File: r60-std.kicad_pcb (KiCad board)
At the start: 2 copper layers, 285.8 x 95.3 mm, 146 parts, among them K0 K_ESC, K0A1 K_0, K0B1 K_MIN, K0C1 K_EQL, K0D1 K_BS, K1 K_1, K10 K_TAB, K11 K_Q, K12 K_W, K13 K_E, K14 K_R, K15 K_T, K16 K_Y, K17 K_U, K18 K_I, K19 K_O, K1A1 K_P, K1B1 K_OBR, K1C1 K_CBR, K1D1 K_BSL, K2 K_2, K20 K_CAP, K21 K_A, K22 K_S, K23 K_D, K24 K_F, K25 K_G, K26 K_H, K27 K_J, K28 K_K, K29 K_L, K2A1 K_COL, K2B1 K_QOT, K2C1 K_ENT, K3 K_3, K30 K_LSH, K31 K_Z, K32 K_X, K33 K_C, K34 K_V, K35 K_B, K36 K_N, K37 K_M, K38 K_COM, K39 K_DOT, K3A1 K_QUE, K3B1 K_RSH, K4 K_4, K40 K_LCL, K41 K_LWN, K42 K_LAL, K45 K_SP, K48 K_RFN, K49 K_RALT, K4A1 K_RWIN, K4B1 K_RCTL, K5 K_5, K6 K_6, K7 K_7, K8 K_8, K9 K_9, P1 USB_B, P2 SPKR, SW1 SW_Push, U1 ATmega32U4-AU, Y1 16MHz

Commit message: Change cut edge holes to slot cuts
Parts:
- removed the REF** at (28.6, 100.0)
- removed the REF** at (314.3, 100.0)
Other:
- outline, holes or cut-outs redrawn
- board text added: "R60 Standard Board Rev 1.1"
- board text removed: "R60 Standard Board Rev A"
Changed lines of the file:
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@@
     (links 230)
     (no_connects 0)
-    (area 22.025 41.274999 320.875 138.420451)
+    (area 28.499999 42.787499 314.400001 138.187501)
     (thickness 1.6)
-    (drawings 11)
+    (drawings 19)
     (tracks 878)
     (zones 0)
-    (modules 146)
+    (modules 144)
     (nets 93)
   )
   (page USLegal)
+  (title_block
+    (title r60-std)
+    (date 2017-08-19)
+    (rev 1.1)
+  )
   (layers
     (0 F.Cu signal)
@@
     (visible_elements FFFFFF7F)
     (pcbplotparams
-      (layerselection 0x010f0_80000001)
+      (layerselection 0x010fc_80000001)
       (usegerberextensions true)
       (excludeedgelayer true)
@@
     (pad 4 thru_hole circle (at 0 0) (size 7 7) (drill oval 5.2 2.7) (layers *.Cu *.Mask))
   )
-  (module Mounting_Holes:MountingHole_2.7mm_M2.5 locked (layer F.Cu)
-    (at 28.575 100.0125)
-    (descr "Mounting Hole 2.7mm, no annular, M2.5")
-    (tags "mounting hole 2.7mm no annular m2.5")
-    (fp_text reference REF** (at 0 -3.7) (layer F.SilkS)
-      (effects (font (size 1 1) (thickness 0.15)))
-    )
-    (fp_text value "" (at 0 3.7) (layer F.Fab)
-      (effects (font (size 1 1) (thickness 0.15)))
-    )
-    (fp_circle (center 0 0) (end 2.7 0) (layer Cmts.User) (width 0.15))
-    (fp_circle (center 0 0) (end 2.95 0) (layer F.CrtYd) (width 0.05))
-    (pad 2 thru_hole oval (at 0 0) (size 12.7 5) (drill oval 10 2.7) (layers *.Cu *.Mask))
-  )
-  (module Mounting_Holes:MountingHole_2.7mm_M2.5 (layer F.Cu)
-    (at 314.325 100.0125)
-    (descr "Mounting Hole 2.7mm, no annular, M2.5")
-    (tags "mounting hole 2.7mm no annular m2.5")
-    (fp_text reference REF** (at 0 -3.7) (layer F.SilkS)
-      (effects (font (size 1 1) (thickness 0.15)))
-    )
-    (fp_text value "" (at 0 3.7) (layer F.Fab)
-      (effects (font (size 1 1) (thickness 0.15)))
-    )
-    (fp_circle (center 0 0) (end 2.7 0) (layer Cmts.User) (width 0.15))
-    (fp_circle (center 0 0) (end 2.95 0) (layer F.CrtYd) (width 0.05))
-    (pad 6 thru_hole oval (at 0 0) (size 12.7 5) (drill oval 10 2.7) (layers *.Cu *.Mask))
-  )
   (module Diodes_THT:D_A-405_P7.62mm_Horizontal (layer F.Cu)
     (at 42.148125 61.9125 180)
@@
       (xy -10.45728 7.127474) (xy -10.4013 7.132925) (xy -10.303849 7.132455)) (layer B.SilkS) (width 0.01))
   )
+  (gr_line (start 314.3238 45.24374) (end 314.3238 98.702578) (layer Edge.Cuts) (width 0.15))
+  (gr_line (start 314.3238 135.73086) (end 314.3238 101.321942) (layer Edge.Cuts) (width 0.15))
+  (gr_arc (start 310.632878 100.01226) (end 310.632878 101.321942) (angle 180) (layer Edge.Cuts) (width 0.15))
+  (gr_line (start 314.3238 101.321942) (end 310.632878 101.321942) (layer Edge.Cuts) (width 0.15))
+  (gr_line (start 314.3238 98.702578) (end 310.632878 98.702578) (layer Edge.Cuts) (width 0.15))
+  (gr_line (start 28.575 98.702578) (end 28.575 45.24374) (layer Edge.Cuts) (width 0.15))
+  (gr_line (start 28.575 135.73086) (end 28.575 101.321942) (layer Edge.Cuts) (width 0.15))
+  (gr_arc (start 32.14686 100.01226) (end 32.265922 98.702578) (angle 170.0419294) (layer Edge.Cuts) (width 0.15))
+  (gr_line (start 28.575 101.321942) (end 32.265922 101.321942) (layer Edge.Cuts) (width 0.15))
+  (gr_line (start 28.575 98.702578) (end 32.265922 98.702578) (layer Edge.Cuts) (width 0.15))
   (gr_text http://github.com/rpedde/r60-std (at 198.501 123.6345) (layer B.SilkS)
     (effects (font (size 1.5 1.5) (thickness 0.3)) (justify mirror))
   )
-  (gr_text "R60 Standard Board Rev A" (at 197.739 126.4285) (layer B.SilkS)
+  (gr_text "R60 Standard Board Rev 1.1" (at 197.739 126.4285) (layer B.SilkS)
     (effects (font (size 1.5 1.5) (thickness 0.3)) (justify mirror))
   )
@@
   )
   (gr_line (start 311.94375 138.1125) (end 30.95625 138.1125) (angle 90) (layer Edge.Cuts) (width 0.15))
-  (gr_line (start 314.325 45.24375) (end 314.325 135.73125) (angle 90) (layer Edge.Cuts) (width 0.15))
   (gr_line (start 30.95625 42.8625) (end 311.94375 42.8625) (angle 90) (layer Edge.Cuts) (width 0.15))
-  (gr_line (start 28.575 135.73125) (end 28.575 45.24375) (angle 90) (layer Edge.Cuts) (width 0.15))
   (gr_arc (start 30.95625 135.73125) (end 30.95625 138.1125) (angle 90) (layer Edge.Cuts) (width 0.15))
   (gr_arc (start 311.94375 135.73125) (end 314.325 135.73125) (angle 90) (layer Edge.Cuts) (width 0.15))

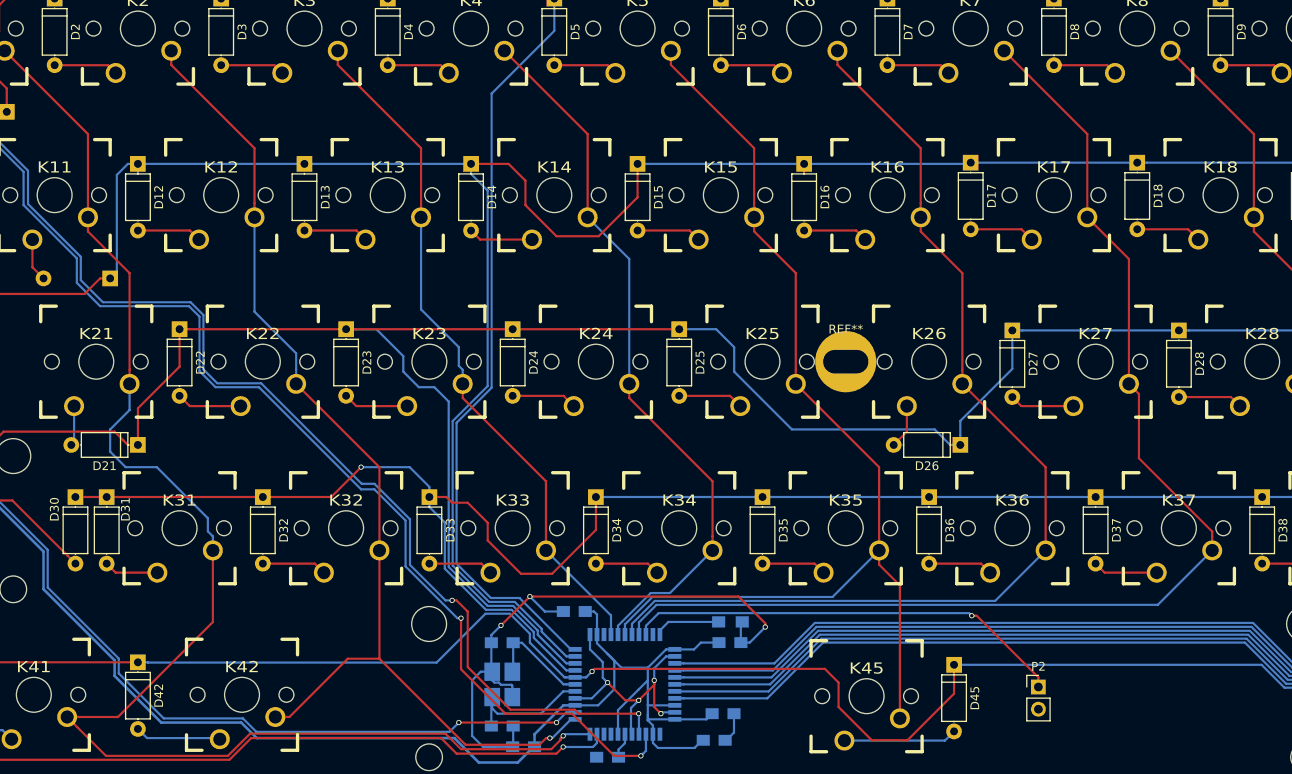
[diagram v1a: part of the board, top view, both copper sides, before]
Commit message: Fix silkscreen, move speaker connector, add speaker hardware
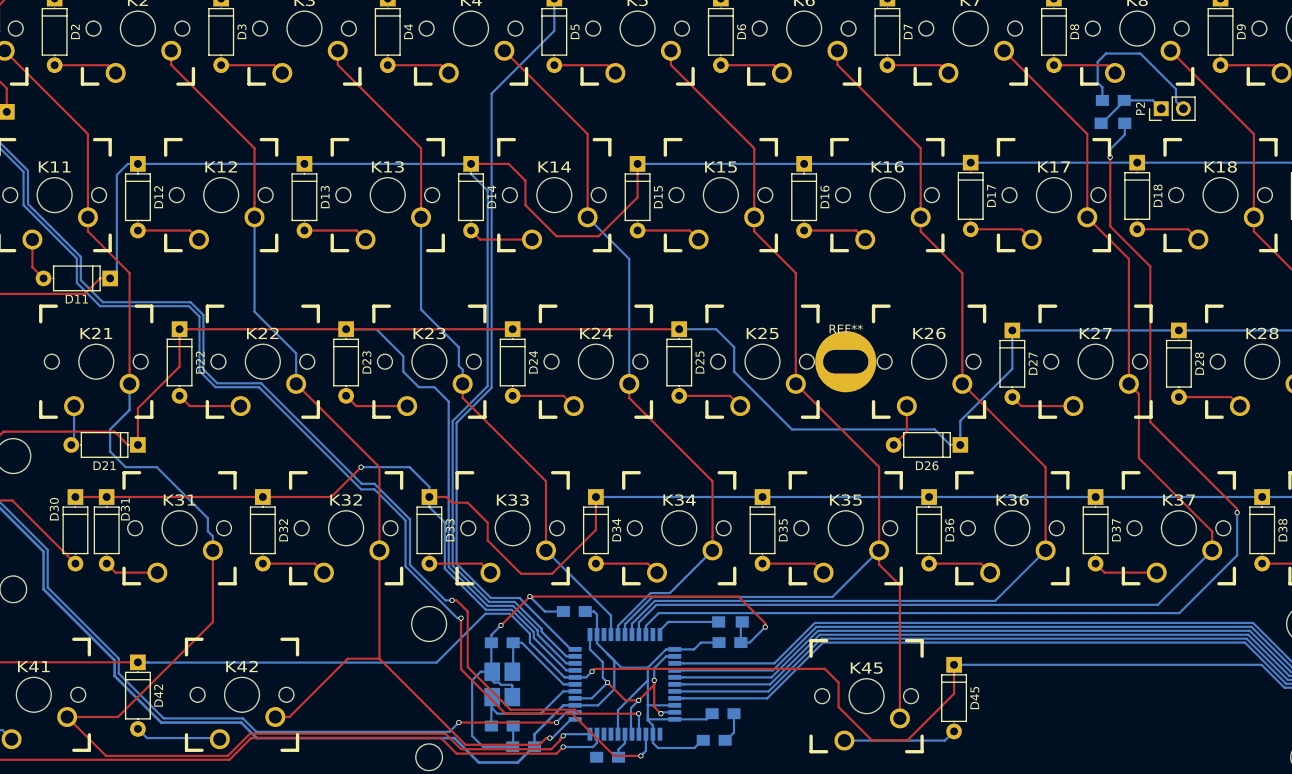
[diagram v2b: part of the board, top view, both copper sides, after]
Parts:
- added C9: .1uF, Capacitors_SMD:C_0805_HandSoldering, B.Cu at (187.8, 60.6)
- added R5: 22, Resistors_SMD:R_0805_HandSoldering, B.Cu at (187.7, 63.2)
- D11: moved to F.Cu
- moved P2 67.6 mm to (193.2, 61.6), turned to 90 degrees
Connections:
- P2 pad 1: Net-(P2-Pad1) -> Net-(C9-Pad1)
- U1 pad 31: Net-(P2-Pad1) -> Net-(R5-Pad1)
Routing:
- net Net-(R5-Pad1): track 0.00 -> 128.1 mm, vias 0 -> 2
- net Net-(P2-Pad1): track 50.6 -> 0.00 mm, vias 1 -> 0
- net GND: track 156.1 -> 174.4 mm
- net Net-(C9-Pad1): track 0.00 -> 8.39 mm
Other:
- board text added: "R60 Standard Board Rev 1.2"
- board text removed: "R60 Standard Board Rev 1.1"

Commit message: start on r2.0 board
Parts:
- C1, C2, C3, C4, C5, C6, C7, C8, C9: footprint Capacitors_SMD:C_0805_HandSoldering -> Capacitors_SMD:C_0805
- D0, D0A1, D0B1, D0C1, D0D1, D1, D10, D11, D12, D13, D14, D15, D16, D17, D18, D19, D1A1, D1B1, D1C1, D1D1, D2, D20, D21, D22, D23, D24, D25, D26, D27, D28, D29, D2A1, D2B1, D2C1, D3, D30, D31, D32, D33, D34, D35, D36, D37, D38, D39, D3A1, D3B1, D4, D40, D41, D42, D45, D48, D49, D4A1, D4B1, D5, D6, D7, D8, D9: footprint Diodes_THT:D_A-405_P7.62mm_Horizontal -> Diodes_SMD:D_SOD-323; moved to B.Cu
- R1, R2, R3, R4, R5: footprint Resistors_SMD:R_0805_HandSoldering -> Resistors_SMD:R_0805
- Y1: footprint Crystals:Crystal_SMD_3225-4pin_3.2x2.5mm_HandSoldering -> Crystals:Crystal_SMD_3225-4pin_3.2x2.5mm
- moved D2C1 23.5 mm to (294.1, 96.4), turned to 180 degrees
- moved D0D1 23.5 mm to (297.7, 58.3), turned to 180 degrees
- moved D3B1 23.5 mm to (289.3, 115.5), turned to 180 degrees
- moved D30 20.2 mm to (51.2, 115.5), turned to 180 degrees
- moved D20 19.4 mm to (46.4, 96.4), turned to 180 degrees
- moved D42 16.3 mm to (89.3, 134.5), turned to 180 degrees
- moved D4B1 16.2 mm to (303.6, 134.5), turned to 180 degrees
- moved D4A1 16.1 mm to (279.8, 134.5), turned to 180 degrees
- moved D17 14.4 mm to (182.2, 77.4), turned to 180 degrees
- moved D1A1 14.4 mm to (239.3, 77.4), turned to 180 degrees
- moved D1B1 14.4 mm to (258.4, 77.4), turned to 180 degrees
- moved D2B1 14.4 mm to (263.1, 96.4), turned to 180 degrees
- moved D18 14.4 mm to (201.2, 77.4), turned to 180 degrees
- moved D19 14.4 mm to (220.3, 77.4), turned to 180 degrees
- moved D1C1 14.4 mm to (277.4, 77.4), turned to 180 degrees
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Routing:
- net GND: track 174.4 -> 77.3 mm, vias 9 -> 7
- net /R4: track 261.4 -> 311.9 mm, vias 1 -> 2
- net Net-(R5-Pad1): track 128.1 -> 159.0 mm
- net Net-(D30-Pad2): track 32.4 -> 3.32 mm
- net /R2: track 330.3 -> 305.5 mm, vias 0 -> 4
- net /R1: track 350.3 -> 332.0 mm, vias 0 -> 4
- net /R0: track 336.4 -> 352.1 mm, vias 0 -> 4
- net Net-(R1-Pad2): track 131.3 -> 146.7 mm
- net Net-(D2C1-Pad2): track 18.2 -> 3.32 mm
- net Net-(D3B1-Pad2): track 18.1 -> 3.32 mm
- net Net-(R2-Pad1): track 136.4 -> 151.0 mm
- net Net-(D0D1-Pad2): track 25.4 -> 11.6 mm
- net Net-(C8-Pad1): track 2.94 -> 15.2 mm
- net /C2: track 121.7 -> 132.6 mm
- net Net-(D1D1-Pad2): track 13.5 -> 3.32 mm
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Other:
- board text added: "R60 Standard Board Rev 2.0"
- board text added: "github.com/rpedde/r60-std"
- board text removed: "R60 Standard Board Rev 1.2"

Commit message: missing some ground pads
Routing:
- net GND: track 77.3 -> 119.8 mm
- net /R3: track 245.8 -> 281.6 mm
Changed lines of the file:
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@@
   (general
     (links 233)
-    (no_connects 3)
+    (no_connects 0)
     (area 28.424529 41.274999 314.475471 138.261701)
     (thickness 1.6)
     (drawings 20)
-    (tracks 1115)
+    (tracks 1131)
     (zones 0)
     (modules 146)
@@
   (gr_arc (start 311.94375 45.24375) (end 311.94375 42.8625) (angle 90) (layer Edge.Cuts) (width 0.15))
   (gr_arc (start 30.95625 45.24375) (end 28.575 45.24375) (angle 90) (layer Edge.Cuts) (width 0.15))
+  (segment (start 49.225 49.8) (end 49.225 51.2) (width 0.25) (layer B.Cu) (net 1))
+  (segment (start 49.225 51.2) (end 49.575 51.55) (width 0.25) (layer B.Cu) (net 1))
+  (segment (start 49.575 51.55) (end 49.575 53.8625) (width 0.25) (layer B.Cu) (net 1))
+  (segment (start 49.575 53.8625) (end 51.775 56.0625) (width 0.25) (layer B.Cu) (net 1))
+  (segment (start 51.775 56.0625) (end 51.775 66.0625) (width 0.25) (layer B.Cu) (net 1))
+  (segment (start 50.05001 67.78749) (end 50.05001 82.665746) (width 0.25) (layer B.Cu) (net 1))
+  (segment (start 51.775 66.0625) (end 50.05001 67.78749) (width 0.25) (layer B.Cu) (net 1))
+  (segment (start 50.05001 82.665746) (end 54.646764 87.2625) (width 0.25) (layer B.Cu) (net 1))
+  (segment (start 54.646764 87.2625) (end 55.175 87.2625) (width 0.25) (layer B.Cu) (net 1))
+  (segment (start 55.175 87.2625) (end 55.175 87.2125) (width 0.25) (layer B.Cu) (net 1))
+  (segment (start 48.425 49.8) (end 49.225 49.8) (width 0.25) (layer B.Cu) (net 1))
   (segment (start 141.275001 134.312503) (end 141.575 134.612502) (width 0.25) (layer F.Cu) (net 1))
   (segment (start 137.574998 130.6125) (end 141.275001 134.312503) (width 0.25) (layer F.Cu) (net 1))
@@
   (segment (start 94.9925 57.4675) (end 95.390625 57.865625) (width 0.25) (layer B.Cu) (net 23))
   (segment (start 95.390625 57.865625) (end 95.390625 58.340625) (width 0.25) (layer B.Cu) (net 23))
+  (segment (start 254.653125 115.490625) (end 257.946875 115.490625) (width 0.25) (layer B.Cu) (net 24))
+  (segment (start 257.946875 115.490625) (end 260.775 112.6625) (width 0.25) (layer B.Cu) (net 24))
+  (segment (start 260.775 112.6625) (end 286.99375 112.6625) (width 0.25) (layer B.Cu) (net 24))
+  (segment (start 286.99375 112.6625) (end 289.821875 115.490625) (width 0.25) (layer B.Cu) (net 24))
+  (segment (start 289.821875 115.490625) (end 290.371875 115.490625) (width 0.25) (layer B.Cu) (net 24))
+  (segment (start 121.303125 115.490625) (end 123.696875 115.490625) (width 0.25) (layer B.Cu) (net 24))
+  (segment (start 123.696875 115.490625) (end 123.925 115.2625) (width 0.25) (layer B.Cu) (net 24))
+  (segment (start 123.925 115.2625) (end 130.975 115.2625) (width 0.25) (layer B.Cu) (net 24))
+  (segment (start 130.975 115.2625) (end 132.325 116.6125) (width 0.25) (layer B.Cu) (net 24))
+  (segment (start 138.68125 116.6125) (end 139.803125 115.490625) (width 0.25) (layer B.Cu) (net 24))
+  (segment (start 132.325 116.6125) (end 138.68125 116.6125) (width 0.25) (layer B.Cu) (net 24))
+  (segment (start 139.803125 115.490625) (end 140.353125 115.490625) (width 0.25) (layer B.Cu) (net 24))
   (segment (start 216.553125 115.490625) (end 217.103125 115.490625) (width 0.25) (layer B.Cu) (net 24))
   (segment (start 217.103125 115.490625) (end 218.23125 114.3625) (width 0.25) (layer B.Cu) (net 24))
@@
   (segment (start 140.903125 115.490625) (end 142.025 116.6125) (width 0.25) (layer B.Cu) (net 24))
   (segment (start 158.853125 115.490625) (end 159.403125 115.490625) (width 0.25) (layer B.Cu) (net 24))
-  (segment (start 121.303125 115.490625) (end 123.696875 115.490625) (width 0.25) (layer B.Cu) (net 24))
-  (segment (start 123.696875 115.490625) (end 126.575 112.6125) (width 0.25) (layer B.Cu) (net 24))
-  (segment (start 126.575 112.6125) (end 128.325 112.6125) (width 0.25) (layer B.Cu) (net 24))
-  (segment (start 128.325 112.6125) (end 132.325 116.6125) (width 0.25) (layer B.Cu) (net 24))
-  (segment (start 132.325 116.6125) (end 138.68125 116.6125) (width 0.25) (layer B.Cu) (net 24))
-  (segment (start 138.68125 116.6125) (end 139.803125 115.490625) (width 0.25) (layer B.Cu) (net 24))
-  (segment (start 139.803125 115.490625) (end 140.353125 115.490625) (width 0.25) (layer B.Cu) (net 24))
   (segment (start 83.203125 115.490625) (end 83.753125 115.490625) (width 0.25) (layer B.Cu) (net 24))
   (segment (start 84.875 116.6125) (end 100.58125 116.6125) (width 0.25) (layer B.Cu) (net 24))

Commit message: switch to 0805 diodes
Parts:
- D0, D0A1, D0B1, D0C1, D0D1, D1, D10, D11, D12, D13, D14, D15, D16, D17, D18, D19, D1A1, D1B1, D1C1, D1D1, D2, D20, D21, D22, D23, D24, D25, D26, D27, D28, D29, D2A1, D2B1, D2C1, D3, D30, D31, D32, D33, D34, D35, D36, D37, D38, D39, D3A1, D3B1, D4, D40, D41, D42, D45, D48, D49, D4A1, D4B1, D5, D6, D7, D8, D9: footprint Diodes_SMD:D_SOD-323 -> Diodes_SMD:D_0805
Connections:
- U1 pad 1: (no net) -> Net-(U1-Pad1)
- U1 pad 25: (no net) -> Net-(U1-Pad25)
- U1 pad 32: (no net) -> Net-(U1-Pad32)
- U1 pad 8: (no net) -> Net-(U1-Pad8)
- U1 pad 9: (no net) -> Net-(U1-Pad9)

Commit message: Expand out 0805 pads on both r and d
re-route some traces as a consequence.
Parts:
- D0, D0A1, D0B1, D0C1, D0D1, D1, D10, D11, D12, D13, D14, D15, D16, D17, D18, D19, D1A1, D1B1, D1C1, D1D1, D2, D20, D21, D22, D23, D24, D25, D26, D27, D28, D29, D2A1, D2B1, D2C1, D3, D30, D31, D32, D33, D34, D35, D36, D37, D38, D39, D3A1, D3B1, D4, D40, D41, D42, D45, D48, D49, D4A1, D4B1, D5, D6, D7, D8, D9: footprint Diodes_SMD:D_0805 -> Keyboard:D_0805
- R1, R2, R3, R4, R5: footprint Resistors_SMD:R_0805 -> Keyboard:RC_0805
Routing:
- net /R1: track 332.0 -> 337.5 mm
- net /R2: track 305.5 -> 309.0 mm
- net /R0: track 352.1 -> 355.1 mm
- net /R3: track 281.6 -> 284.3 mm
- net /R4: track 311.9 -> 313.3 mm

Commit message: add ISO and stepped capslock support
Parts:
- added D2D1: D, Keyboard:D_0805, B.Cu at (290.5, 84.5)
- added D3C1: D, Keyboard:D_0805, B.Cu at (289.3, 115.5)
- added K20-S1: CAPS, Keyboard:CHERRY_PCB_125H, F.Cu at (40.5, 90.5)
- added K2D1: ENTER, Keyboard:CHERRY_PCB_225H, F.Cu at (292.9, 90.5)
- added K2D2: ISOENTER, Keyboard:CHERRY_PCB_200H, F.Cu at (302.4, 81.0)
- added K30-I1: ISOLSHIFT, Keyboard:CHERRY_PCB_125H, F.Cu at (40.5, 109.5)
- added K3C1: RSHIFT, Keyboard:CHERRY_PCB_275H, F.Cu at (288.1, 109.5)
- K0: value K_ESC -> ESC
- K0A1: value K_0 -> 0
- K0B1: value K_MIN -> MINUS
- K0C1: value K_EQL -> EQUAL
- K0D1: value K_BS -> BACKSP
- K1: value K_1 -> 1
- K10: value K_TAB -> TAB
- K11: value K_Q -> Q
- K12: value K_W -> W
- K13: value K_E -> E
- K14: value K_R -> R
- K15: value K_T -> T
- K16: value K_Y -> Y
- K17: value K_U -> U
- K18: value K_I -> I
- K19: value K_O -> O
- K1A1: value K_P -> P
- K1B1: value K_OBR -> LBRACE
- K1C1: value K_CBR -> RBRACE
- K1D1: value K_BSL -> BS_PIPE
- K2: value K_2 -> 2
- K20: value K_CAP -> CAPS
- K21: value K_A -> A
- K22: value K_S -> S
- K23: value K_D -> D
- K24: value K_F -> F
- K25: value K_G -> G
- K26: value K_H -> H
- K27: value K_J -> J
- K28: value K_K -> K
- K29: value K_L -> L
- K2A1: value K_COL -> COLON
- K2B1: value K_QOT -> QUOTE
- K2C1: value K_ENT -> ISOHASH; footprint Keyboard:CHERRY_PCB_225H -> Keyboard:CHERRY_PCB_100H
- K3: value K_3 -> 3
- K30: value K_LSH -> LSHIFT
- K31: value K_Z -> ISOPIPE
- K32: value K_X -> Z
- K33: value K_C -> X
- K34: value K_V -> C
- K35: value K_B -> V
- K36: value K_N -> B
- K37: value K_M -> N
- K38: value K_COM -> M
- K39: value K_DOT -> COMMA
- K3A1: value K_QUE -> DOT
- K3B1: value K_RSH -> SLASH; footprint Keyboard:CHERRY_PCB_275H -> Keyboard:CHERRY_PCB_100H
- K4: value K_4 -> 4
- K40: value K_LCL -> LCTL
- K41: value K_LWN -> LWIN
- K42: value K_LAL -> LALT
- K45: value K_SP -> SPACE
- K48: value K_RFN -> RALT
- K49: value K_RALT -> RWIN
- K4A1: value K_RWIN -> RGUI
- K4B1: value K_RCTL -> RCTL
- K5: value K_5 -> 5
- K6: value K_6 -> 6
- K7: value K_7 -> 7
- K8: value K_8 -> 8
- K9: value K_9 -> 9
- moved D3B1 35.9 mm to (253.4, 115.5)
- moved K3B1 35.7 mm to (252.4, 109.5)
- moved D36 19.2 mm to (158.2, 115.5)
- moved D39 19.2 mm to (215.3, 115.5)
- moved D35 19.1 mm to (139.3, 115.5)
- moved D37 19.1 mm to (177.4, 115.5)
- moved D38 19.1 mm to (196.5, 115.5)
- moved D3A1 19.1 mm to (234.6, 115.5)
- moved K34 19.1 mm to (119.1, 109.5)
- moved K36 19.1 mm to (157.2, 109.5)
- moved K38 19.1 mm to (195.3, 109.5)
- moved K39 19.1 mm to (214.3, 109.5)
- moved K31 19.1 mm to (61.9, 109.5)
- moved D32 19.0 mm to (82.2, 115.5)
- moved D33 19.0 mm to (101.2, 115.5)
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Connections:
- U1 pad 1: Net-(U1-Pad1) -> (no net)
- U1 pad 25: Net-(U1-Pad25) -> (no net)
- U1 pad 32: Net-(U1-Pad32) -> (no net)
- U1 pad 8: Net-(U1-Pad8) -> (no net)
- U1 pad 9: Net-(U1-Pad9) -> (no net)
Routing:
- net Net-(D2D1-Pad2): track 0.00 -> 19.9 mm
- net /C7: track 139.7 -> 120.7 mm
- net /C13: track 236.2 -> 254.5 mm
- net /C3: track 80.1 -> 97.0 mm, vias 1 -> 2
- net /C0: track 176.7 -> 191.0 mm
- net /C11: track 274.7 -> 262.1 mm
- net /R3: track 284.3 -> 295.3 mm
- net /R1: track 337.5 -> 327.1 mm
- net /C8: track 181.8 -> 191.3 mm
- net Net-(D30-Pad2): track 3.32 -> 12.8 mm
- net /C6: track 122.1 -> 112.6 mm
- net /C10: track 230.4 -> 237.5 mm
- net /C12: track 233.1 -> 228.0 mm
- net /C9: track 204.1 -> 209.3 mm, vias 2 -> 3
- net /C2: track 132.6 -> 127.5 mm
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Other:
- board text added: "R60 Standard Board Rev 3.0"
- board text removed: "R60 Standard Board Rev 2.0"
